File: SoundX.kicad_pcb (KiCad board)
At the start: 2 copper layers, 60.8 x 99.9 mm, 51 parts, among them CN1 EDGE_CONN, CN2 RAW_AUDIO_OUT, CN3 CONN_MIDI_IN, CN4 CONN_MIDI_OUT, U1 GAL20V8, U2 MOS_6551_ACIA, U3 YM3526, U4 6N138, U6 YM3014, U7 LM324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

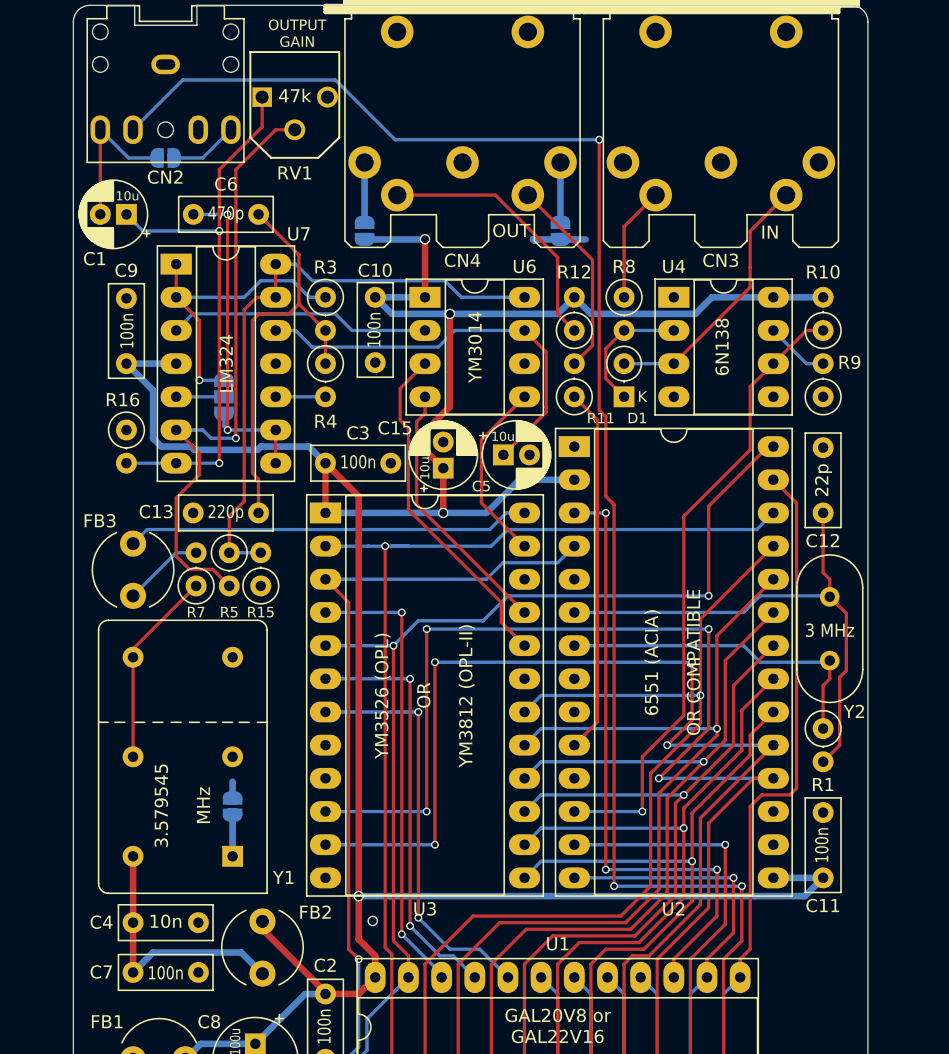
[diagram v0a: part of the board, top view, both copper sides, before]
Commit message: Move C13 up
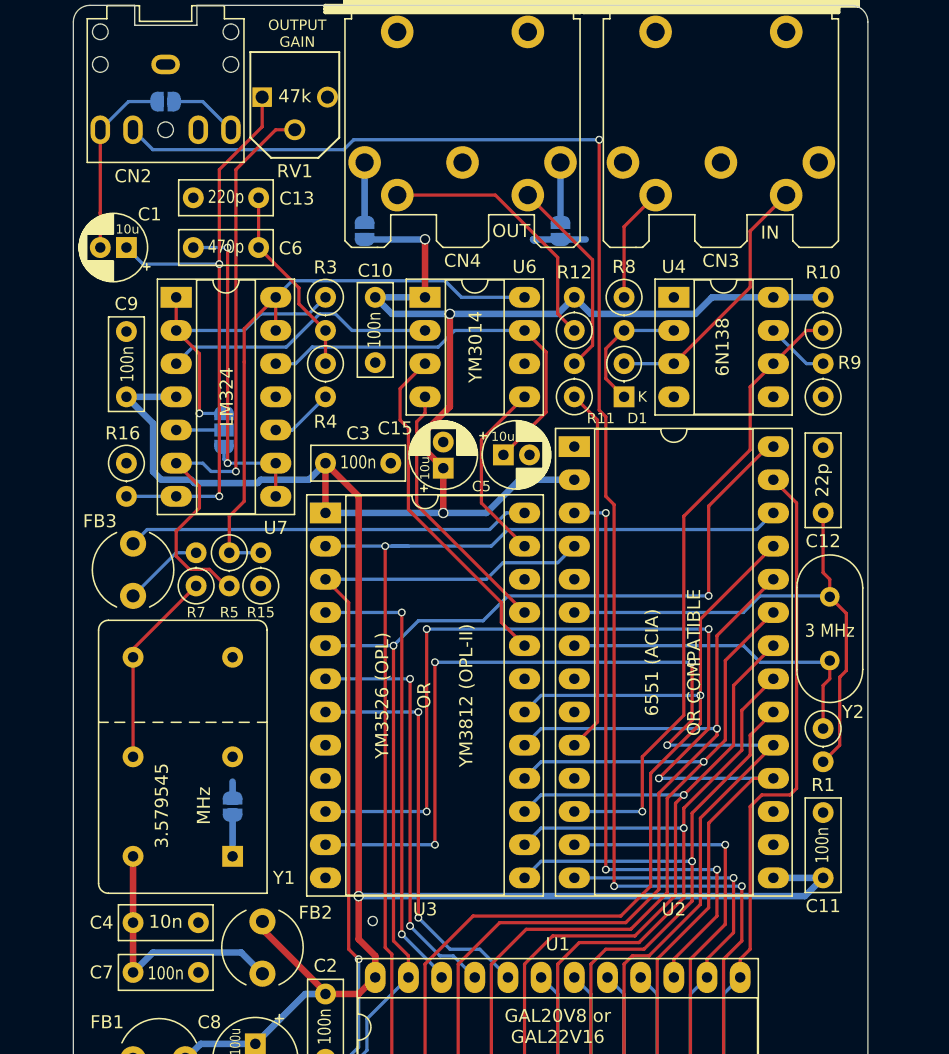
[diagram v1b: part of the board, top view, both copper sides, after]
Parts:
- moved C13 24.1 mm to (136.0, 62.9)
- moved JP2 4.32 mm to (128.9, 55.5)
- moved C9 2.54 mm to (125.9, 78.1)
- moved R16 2.54 mm to (125.9, 83.2)
- moved U7 2.54 mm to (129.7, 70.5)
- moved C1 2.54 mm to (125.9, 66.7)
- moved C6 2.54 mm to (136.0, 66.7)
- moved JP5 2.54 mm to (133.3, 80.6)
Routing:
- net Net-(C13-Pad1): track 32.6 -> 14.8 mm
- net Net-(C1-Pad2): track 11.7 -> 14.4 mm
- net Net-(C1-Pad1): track 43.5 -> 46.0 mm
- net /ext_audio: track 135.8 -> 133.3 mm
- net Net-(U6-Pad2): track 20.1 -> 21.2 mm
- net Net-(R4-Pad2): track 3.81 -> 4.86 mm
- net Net-(R15-Pad2): track 46.9 -> 46.2 mm

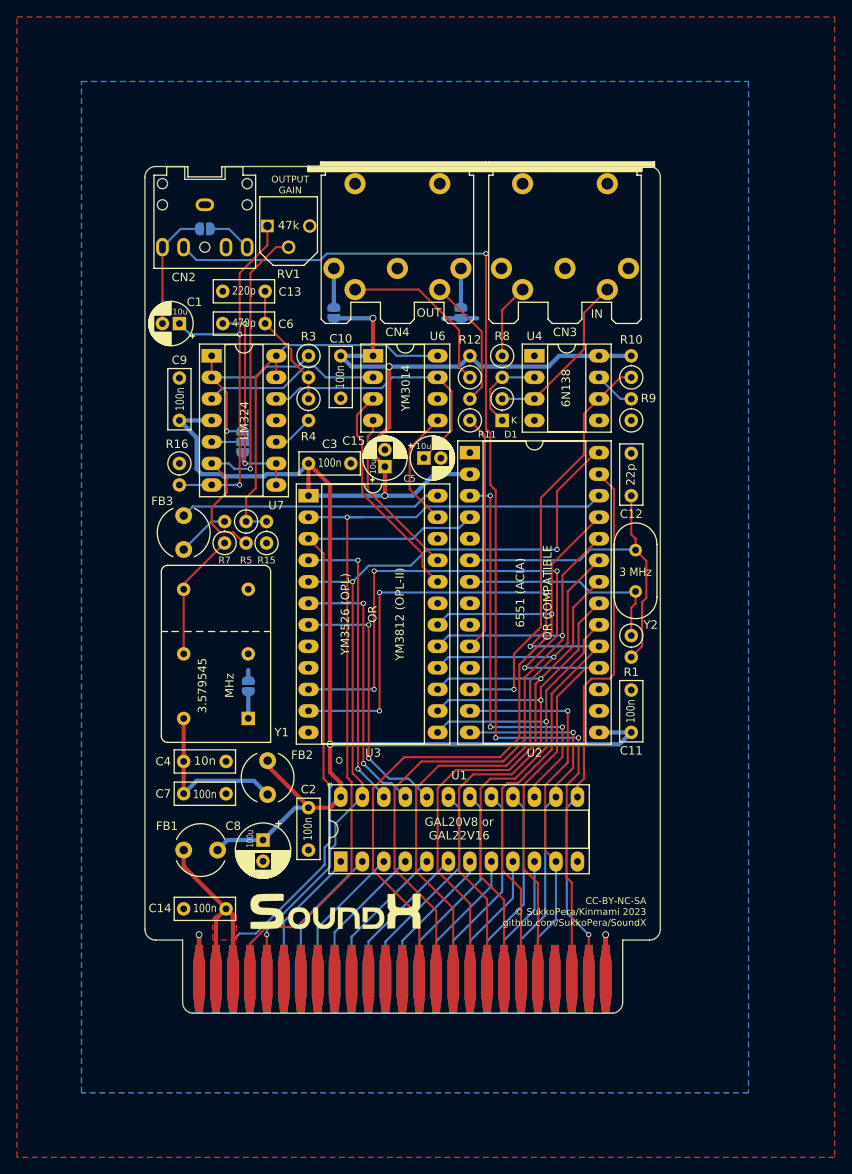
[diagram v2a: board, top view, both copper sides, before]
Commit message: Switch to 2 oscillators (and KiCad 8)
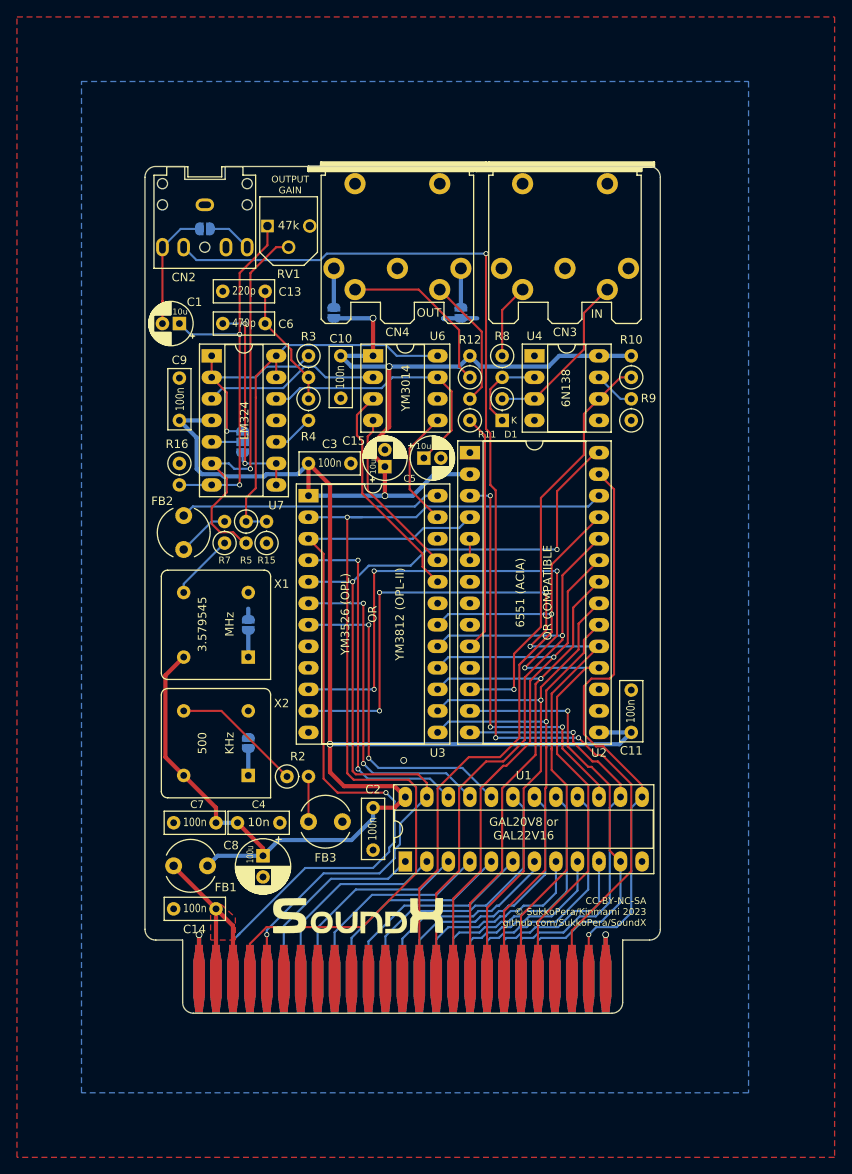
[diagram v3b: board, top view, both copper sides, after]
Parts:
- removed C12: 22p, Capacitor_THT:C_Disc_D7.0mm_W2.5mm_P5.00mm
- removed the FB2 at (136.3, 122.3)
- removed R1: 1M, Resistor_THT:R_Axial_DIN0207_L6.3mm_D2.5mm_P2.54mm_Vertical
- removed Y2: 3M, Crystal:Crystal_HC49-U_Vertical
- added FB3: FERRITE, Inductor_THT:L_Radial_D6.0mm_P4.00mm, F.Cu at (145.1, 125.5)
- added JP6: JMP_OSC2_PIN1, Jumper:SolderJumper-2_P1.3mm_Open_RoundedPad1.0x1.5mm, B.Cu at (134.0, 116.2)
- added R2: 47, Resistor_THT:R_Axial_DIN0207_L6.3mm_D2.5mm_P2.54mm_Vertical, F.Cu at (138.6, 120.1)
- added X2: 500 kHz, Oscillator:Oscillator_DIP-8, F.Cu at (134.0, 120.0)
- JP1: value JMP_OSC_PIN1 -> JMP_OSC1_PIN1
- X1: renamed from Y1; footprint SoundX:Oscillator_DIP-8+14 -> Oscillator:Oscillator_DIP-8
- moved C4 9.63 mm to (132.7, 125.6)
- moved C2 7.62 mm to (148.7, 123.8)
- moved U1 7.62 mm to (152.5, 130.2)
- moved JP1 7.24 mm to (134.0, 102.2)
- moved X1 7.24 mm to (134.0, 106.0)
- moved C7 5.13 mm to (130.2, 125.6), turned to 180 degrees
- moved V1 2.71 mm to (146.9, 136.5)
- moved FB1 2.21 mm to (125.2, 130.7)
- moved C8 1.86 mm to (135.7, 129.5)
- moved C14 1.19 mm to (130.2, 135.8)
- renumbered FB3 to FB2
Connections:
- net /clock renamed /clock_ym
- net /r_~w renamed /r_~{w}
- net /~irq renamed /~{irq}
- net /~midi_cs renamed /~{midi_cs}
- net /~reset renamed /~{reset}
- net /~ym_cs renamed /~{ym_cs}
- net /~ym_rd renamed /~{ym_rd}
- C4 pad 1: Net-(C4-Pad1) -> +5V
- C7 pad 1: Net-(C4-Pad1) -> +5V
- CN1 pad 10: Net-(CN1-Pad10) -> unconnected-(CN1-/CS0-Pad10)
- CN1 pad 11: Net-(CN1-Pad11) -> unconnected-(CN1-/CAS-Pad11)
- CN1 pad 12: Net-(CN1-Pad12) -> unconnected-(CN1-MUX-Pad12)
- CN1 pad 13: Net-(CN1-Pad13) -> unconnected-(CN1-BA-Pad13)
- CN1 pad 22: Net-(CN1-Pad22) -> unconnected-(CN1-AEC-Pad22)
- CN1 pad 6: Net-(CN1-Pad6) -> unconnected-(CN1-C1HI-Pad6)
- CN1 pad 7: Net-(CN1-Pad7) -> unconnected-(CN1-C2LOW-Pad7)
- CN1 pad 8: Net-(CN1-Pad8) -> unconnected-(CN1-C2HI-Pad8)
- CN1 pad 9: Net-(CN1-Pad9) -> unconnected-(CN1-/CS1-Pad9)
- CN1 pad AA: Net-(CN1-PadAA) -> unconnected-(CN1-NC-PadAA)
- CN1 pad B: Net-(CN1-PadB) -> unconnected-(CN1-C1LOW-PadB)
- CN1 pad BB: Net-(CN1-PadBB) -> unconnected-(CN1-NC-PadBB)
- CN1 pad D: Net-(CN1-PadD) -> unconnected-(CN1-/RAS-PadD)
- CN1 pad E: Net-(CN1-PadE) -> unconnected-(CN1-PHI0-PadE)
- CN1 pad Z: Net-(CN1-PadZ) -> unconnected-(CN1-NC-PadZ)
- CN2 pad RN: Net-(CN2-PadRN) -> unconnected-(CN2-PadRN)
- CN3 pad 1: Net-(CN3-Pad1) -> unconnected-(CN3-Pad1)
- CN3 pad 2: Net-(CN3-Pad2) -> unconnected-(CN3-Pad2)
- CN3 pad 3: Net-(CN3-Pad3) -> unconnected-(CN3-Pad3)
- R7 pad 1: Net-(R7-Pad1) -> Net-(X1-OUT)
- RV1 pad 3: Net-(RV1-Pad3) -> unconnected-(RV1-Pad3)
- U2 pad 11: Net-(U2-Pad11) -> unconnected-(U2-~{DTR}-Pad11)
- U2 pad 5: Net-(U2-Pad5) -> /clock_acia
- U2 pad 6: /q+ -> /clock_acia
- U2 pad 7: /q- -> unconnected-(U2-XTLO-Pad7)
- U2 pad 8: Net-(U2-Pad8) -> unconnected-(U2-~{RTS}-Pad8)
- U3 pad 19: Net-(U3-Pad19) -> unconnected-(U3-NC-Pad19)
- U3 pad 22: Net-(U3-Pad22) -> unconnected-(U3-NC-Pad22)
- U3 pad 8: Net-(U3-Pad8) -> unconnected-(U3-NC-Pad8)
- U3 pad 9: Net-(U3-Pad9) -> unconnected-(U3-NC-Pad9)
- U4 pad 1: Net-(U4-Pad1) -> unconnected-(U4-NC-Pad1)
- U4 pad 4: Net-(U4-Pad4) -> unconnected-(U4-NC-Pad4)
- X1 pad 8: Net-(R7-Pad1) -> +5V
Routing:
- net /q+: track 40.5 -> 0.00 mm
- net +5V: track 221.2 -> 261.5 mm
- net /q-: track 25.4 -> 0.00 mm
- net Net-(C4-Pad1): track 20.1 -> 0.00 mm
- net Net-(X2-OUT): track 0.00 -> 15.4 mm
- net Net-(R7-Pad1): track 15.1 -> 0.00 mm
- net /~{irq}: track 98.4 -> 113.0 mm
- net /r_~{w}: track 96.6 -> 111.1 mm
- net /~{reset}: track 79.0 -> 92.5 mm
- net /d7: track 88.4 -> 79.4 mm
- net /a1: track 43.9 -> 52.5 mm
- net /d6: track 84.9 -> 76.3 mm
- net /a6: track 16.5 -> 24.8 mm
- net /d5: track 79.1 -> 71.0 mm
- net /a9: track 25.6 -> 33.6 mm
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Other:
- net class Default removed
- net class Power removed
- board text added: "500 KHz"
- board text removed: "3 MHz"

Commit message: Version with MC6850 should be ready
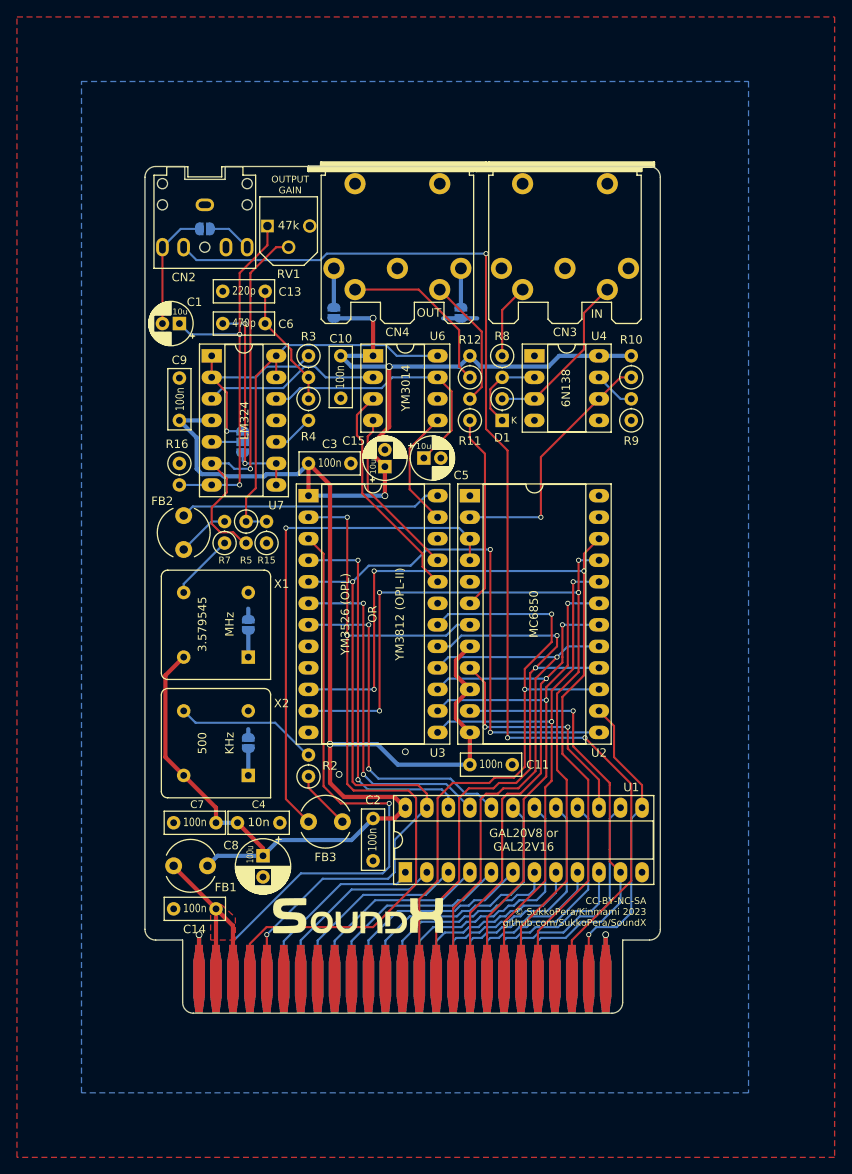
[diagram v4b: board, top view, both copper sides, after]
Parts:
- CN2: value RAW_AUDIO_OUT -> AUDIO_OUT
- U2: value MOS_6551_ACIA -> MC6850; footprint Package_DIP:DIP-28_W15.24mm_Socket_LongPads -> Package_DIP:DIP-24_W15.24mm_Socket_LongPads
- moved C11 19.4 mm to (160.1, 118.7), turned to 0 degrees
- moved U2 5.08 mm to (160.1, 87.0)
- moved FB3 4.00 mm to (141.1, 125.5), turned to 0 degrees
- moved R2 2.54 mm to (141.1, 120.1), turned to 90 degrees
- moved C2 1.27 mm to (148.7, 125.1)
- moved U1 1.27 mm to (152.5, 131.4)
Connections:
- R2 pad 1: Net-(X2-OUT) -> Net-(FB3-Pad2)
- R2 pad 2: Net-(FB3-Pad2) -> Net-(X2-OUT)
- U2 pad 10: /txd_ttl -> +5V
- U2 pad 11: unconnected-(U2-~{DTR}-Pad11) -> /a0
- U2 pad 12: /rxd_ttl -> +5V
- U2 pad 13: /a0 -> /r_~{w}
- U2 pad 14: /a1 -> /phi2
- U2 pad 15: +5V -> /d7
- U2 pad 16: GND -> /d6
- U2 pad 17: GND -> /d5
- U2 pad 18: /d0 -> /d4
- U2 pad 19: /d1 -> /d3
- U2 pad 2: +5V -> /rxd_ttl
- U2 pad 21: /d3 -> /d1
- U2 pad 22: /d4 -> /d0
- U2 pad 23: /d5 -> GND
- U2 pad 24: /d6 -> GND
- U2 pad 3: /~{midi_cs} -> /clock_acia
- U2 pad 4: /~{reset} -> /clock_acia
- U2 pad 5: /clock_acia -> unconnected-(U2-~{RTS}-Pad5)
- U2 pad 6: /clock_acia -> /txd_ttl
- U2 pad 7: unconnected-(U2-XTLO-Pad7) -> /~{irq}
- U2 pad 8: unconnected-(U2-~{RTS}-Pad8) -> +5V
- U2 pad 9: GND -> /~{midi_cs}
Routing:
- net /clock_acia: track 2.54 -> 60.6 mm, vias 0 -> 1
- net /phi2: track 70.4 -> 36.5 mm
- net /a1: track 52.5 -> 28.6 mm, vias 1 -> 0
- net /~{midi_cs}: track 48.3 -> 27.3 mm, vias 3 -> 2
- net /~{reset}: track 92.5 -> 72.5 mm
- net /rxd_ttl: track 48.5 -> 30.1 mm
- net +5V: track 261.5 -> 243.3 mm
- net /~{irq}: track 113.0 -> 96.7 mm, vias 1 -> 2
- net /r_~{w}: track 111.1 -> 124.6 mm, vias 3 -> 4
- net /d2: track 59.8 -> 67.3 mm, vias 1 -> 2
- net /d5: track 71.0 -> 65.0 mm
- net /txd_ttl: track 28.1 -> 23.1 mm
- net /d6: track 76.3 -> 71.4 mm, vias 1 -> 2
- net /d0: track 108.7 -> 103.9 mm, vias 4 -> 3
- net /d7: track 79.4 -> 76.1 mm, vias 1 -> 2
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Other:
- board text added: "MC6850"
- board text added: "V2"
- board text removed: "6551 (ACIA) OR COMPATIBLE"
- board text removed: "V1"
